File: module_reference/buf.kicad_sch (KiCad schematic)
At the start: 48 parts, among them J401 Conn_01x01, Q401 MMBT3904, U401 ADA4523, U402 ADG5401F, U403 ADA4523, U404 ADA4523, U405 D60V0L4B10LP

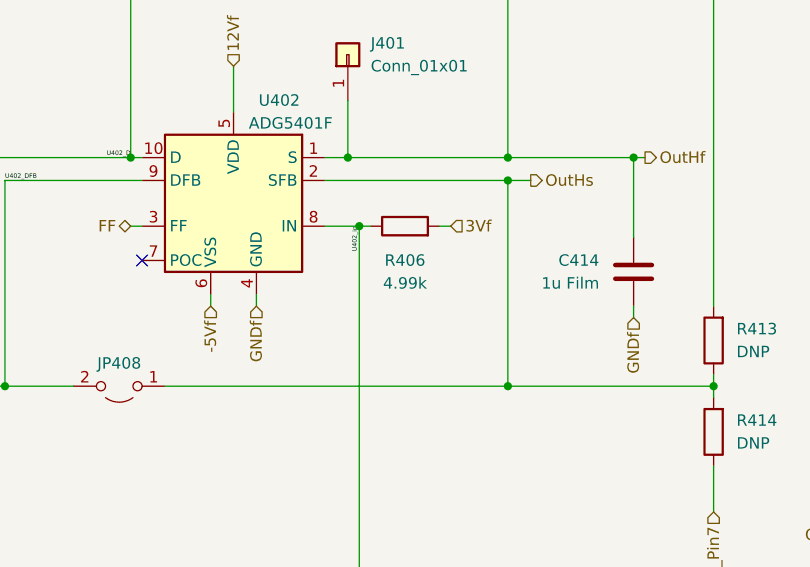
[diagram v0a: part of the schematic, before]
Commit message: adds cost estimate csv
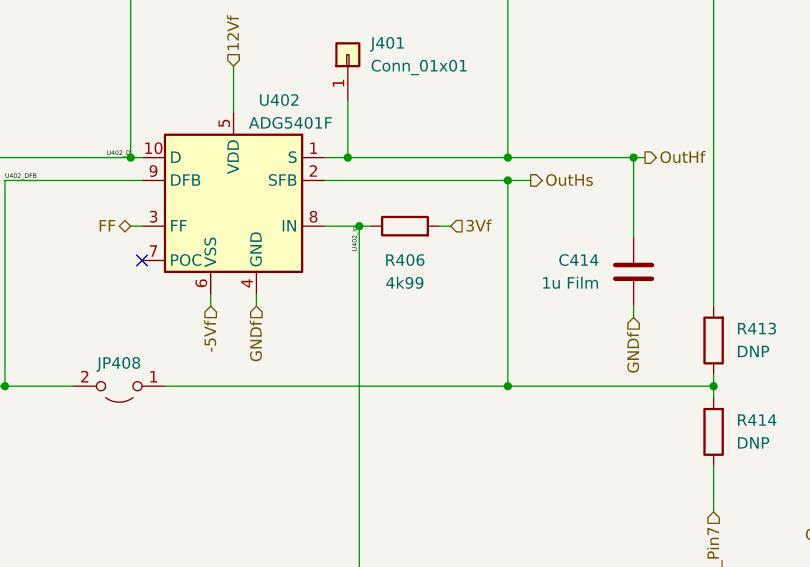
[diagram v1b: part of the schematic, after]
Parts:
- R406: value 4.99k -> 4k99
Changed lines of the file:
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@@
     (in_bom yes) (on_board yes) (fields_autoplaced)
     (property "Reference" "R406" (id 0) (at 198.12 69.85 90))
-    (property "Value" "4.99k" (id 1) (at 198.12 72.39 90))
+    (property "Value" "4k99" (id 1) (at 198.12 72.39 90))
     (property "Footprint" "Resistor_SMD:R_0805_2012Metric" (id 2) (at 198.12 67.818 90)
       (effects (font (size 1.27 1.27)) hide)
